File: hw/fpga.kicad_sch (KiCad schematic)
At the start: 1 part, among them U3 ICE40UL1K-CM36AITR

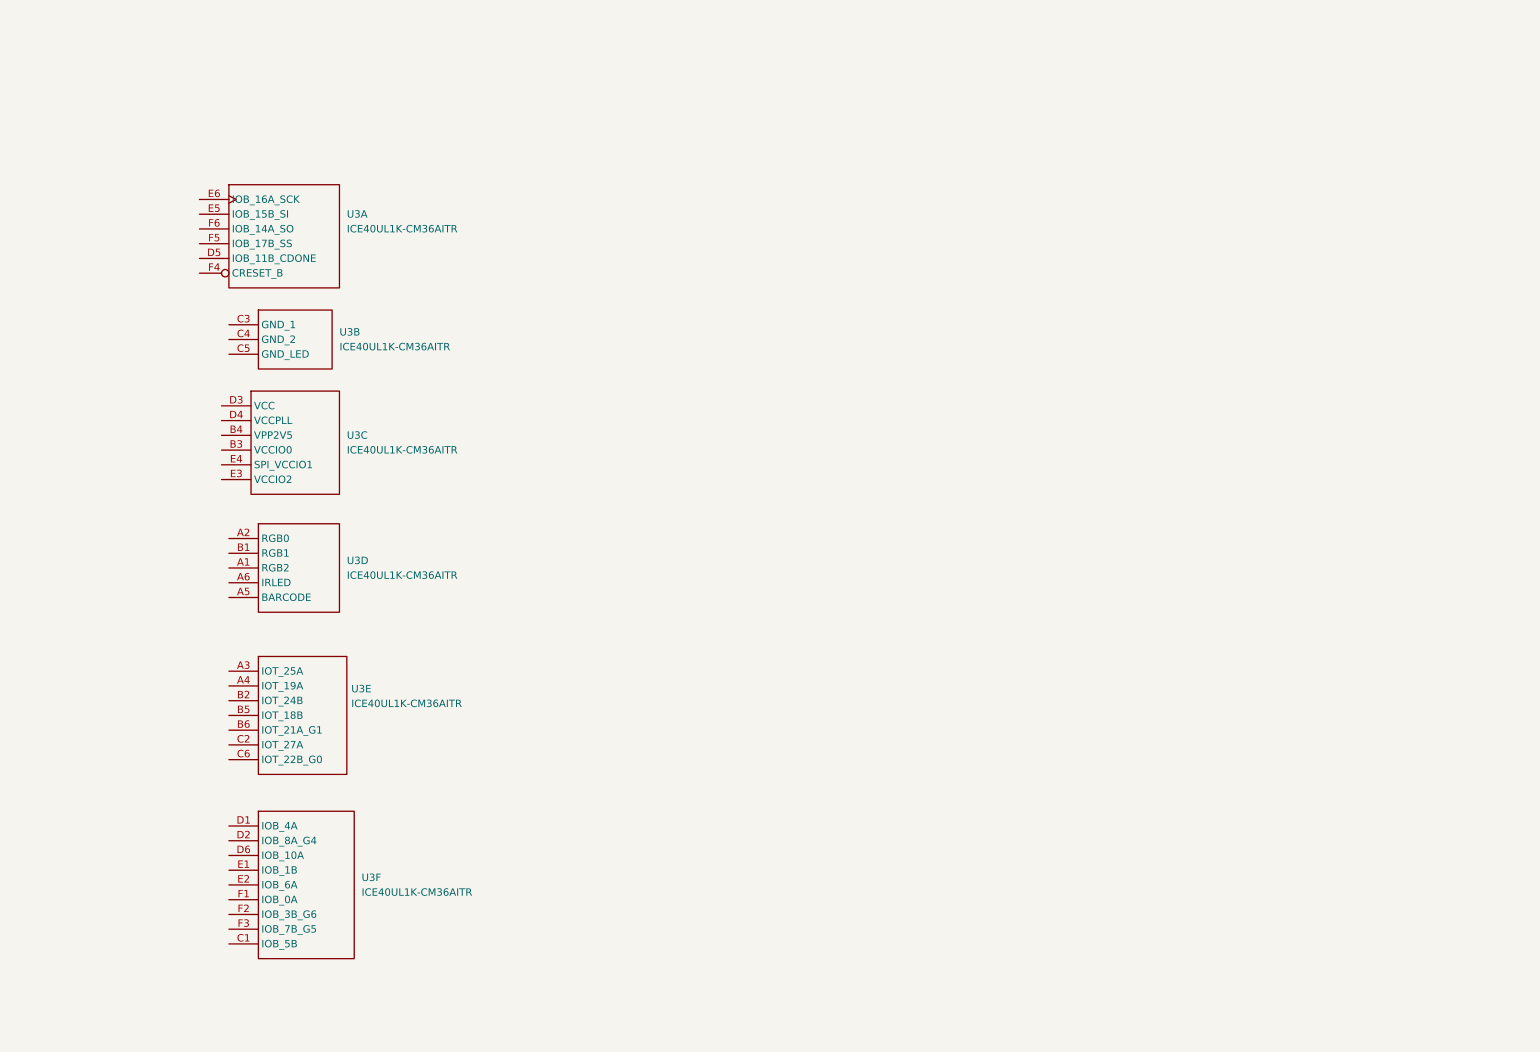
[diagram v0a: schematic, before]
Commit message: Place FPGA
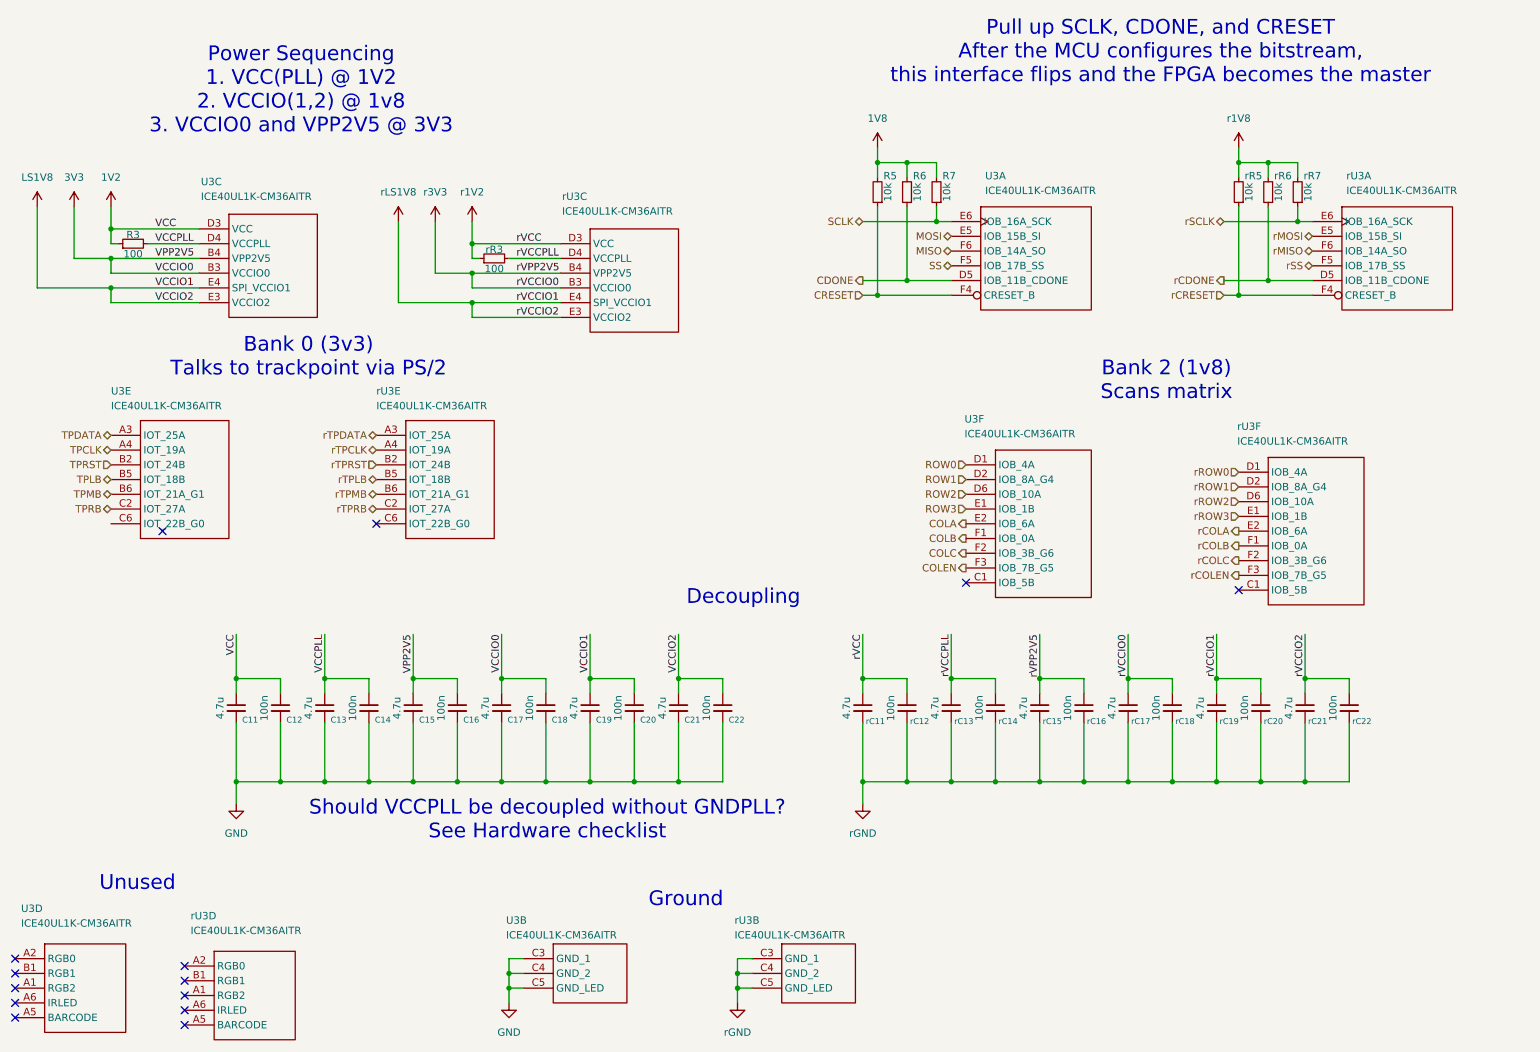
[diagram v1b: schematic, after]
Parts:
- added C11, C13, C15, C17, C19, C21, rC11, rC13, rC15, rC17, rC19, rC21: 4.7u, symbol Alidade:C
- added C12, C14, C16, C18, C20, C22, rC12, rC14, rC16, rC18, rC20, rC22: 100n, symbol Alidade:C
- added R3, rR3: 100, symbol Alidade:R
- added R5, R6, R7, rR5, rR6, rR7: 10k, symbol Alidade:R
- added rU3: ICE40UL1K-CM36AITR, Alidade:BGA36C40P6X6_250X250X100, symbol Alidade:ICE40UL1K-CM36AITR
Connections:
- net 3V3: now reaches U3.B3 (VCCIO0)
- net 3V3: now also U3.B4 (VPP2V5), C15.1, C16.1, C17.1, C18.1
- net 1V2: now reaches U3.D3 (VCC)
- net 1V2: now also C11.1, C12.1, R3.1
- net VCCPLL: now reaches U3.D4 (VCCPLL)
- net VCCPLL: now also C13.1, C14.1, R3.2
- net LS1V8: now reaches U3.E3 (VCCIO2)
- net LS1V8: now also U3.E4 (SPI_VCCIO1), C19.1, C20.1, C21.1, C22.1
- net TPDATA: now reaches U3.A3 (IOT_25A)
- net TPCLK: now reaches U3.A4 (IOT_19A)
- net TPRST: now reaches U3.B2 (IOT_24B)
- net TPLB: now reaches U3.B5 (IOT_18B)
- net TPMB: now reaches U3.B6 (IOT_21A_G1)
- net TPRB: now reaches U3.C2 (IOT_27A)
- net CDONE: now reaches U3.D5 (IOB_11B_CDONE)
- net CDONE: now also R6.1
- net MOSI: now reaches U3.E5 (IOB_15B_SI)
- net SCLK: now reaches U3.E6 (IOB_16A_SCK)
- net SCLK: now also R7.1
- net CRESET: now reaches U3.F4 (CRESET_B)
- net CRESET: now also R5.1
- net SS: now reaches U3.F5 (IOB_17B_SS)
- net MISO: now reaches U3.F6 (IOB_14A_SO)
- net ROW0: now reaches U3.D1 (IOB_4A)
- net ROW1: now reaches U3.D2 (IOB_8A_G4)
- net ROW2: now reaches U3.D6 (IOB_10A)
- net ROW3: now reaches U3.E1 (IOB_1B)
- net COLA: now reaches U3.E2 (IOB_6A)
- net COLB: now reaches U3.F1 (IOB_0A)
- net COLC: now reaches U3.F2 (IOB_3B_G6)
- net COLEN: now reaches U3.F3 (IOB_7B_G5)
- net GND: now reaches U3.C3 (GND_1)
- net GND: now also U3.C4 (GND_2), U3.C5 (GND_LED), C11.2, C12.2, C13.2, C14.2, C15.2, C16.2, C17.2, C18.2, C19.2, C20.2, C21.2, C22.2
- new net 1V8: R5.2, R6.2, R7.2
- new net r1V2: rC11.1, rC12.1, rR3.1, rU3.D3 (VCC)
- new net r1V8: rR5.2, rR6.2, rR7.2
- new net r3V3: rC15.1, rC16.1, rC17.1, rC18.1, rU3.B3 (VCCIO0), rU3.B4 (VPP2V5)
- new net rCDONE: rR6.1, rU3.D5 (IOB_11B_CDONE)
- new net rCOLA: rU3.E2 (IOB_6A)
- new net rCOLB: rU3.F1 (IOB_0A)
- new net rCOLC: rU3.F2 (IOB_3B_G6)
- new net rCOLEN: rU3.F3 (IOB_7B_G5)
- new net rCRESET: rR5.1, rU3.F4 (CRESET_B)
- new net rGND: rC11.2, rC12.2, rC13.2, rC14.2, rC15.2, rC16.2, rC17.2, rC18.2, rC19.2, rC20.2, rC21.2, rC22.2, rU3.C3 (GND_1), rU3.C4 (GND_2), rU3.C5 (GND_LED)
- new net rLS1V8: rC19.1, rC20.1, rC21.1, rC22.1, rU3.E3 (VCCIO2), rU3.E4 (SPI_VCCIO1)
- new net rMISO: rU3.F6 (IOB_14A_SO)
- new net rMOSI: rU3.E5 (IOB_15B_SI)
- new net rROW0: rU3.D1 (IOB_4A)
- new net rROW1: rU3.D2 (IOB_8A_G4)
- new net rROW2: rU3.D6 (IOB_10A)
- new net rROW3: rU3.E1 (IOB_1B)
- new net rSCLK: rR7.1, rU3.E6 (IOB_16A_SCK)
- new net rSS: rU3.F5 (IOB_17B_SS)
- new net rTPCLK: rU3.A4 (IOT_19A)
- new net rTPDATA: rU3.A3 (IOT_25A)
- new net rTPLB: rU3.B5 (IOT_18B)
- new net rTPMB: rU3.B6 (IOT_21A_G1)
- new net rTPRB: rU3.C2 (IOT_27A)
- new net rTPRST: rU3.B2 (IOT_24B)
- new net rVCCPLL: rC13.1, rC14.1, rR3.2, rU3.D4 (VCCPLL)
- no-connect marks 0 -> 14
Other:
- note added: "Bank 0 (3v3) Talks to trackpoint via PS/2"
- note added: "Bank 2 (1v8) Scans matrix"
- note added: "Decoupling"
- note added: "Ground"
- note added: "Power Sequencing 1. VCC(PLL) @ 1V2 2. VCCIO(1,2) @ 1v8 3. VCCIO0 and VPP2V5 @ 3V3"
- note added: "Pull up SCLK, CDONE, and CRESET After the MCU configures the bitstream, this interface flips and the FPGA becomes the master"
- note added: "Should VCCPLL be decoupled without GNDPLL? See Hardware checklist"
- note added: "Unused"
- moved on the sheet: U3A, U3B, U3C, U3D, U3E, U3F

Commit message: Sheet pins
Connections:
- net MISO renamed FPGAMISO
- net MOSI renamed FPGAMOSI
- net SCLK renamed FPGASCLK
- net SS renamed FPGACS
- net rMISO renamed rFPGAMISO
- net rMOSI renamed rFPGAMOSI
- net rSCLK renamed rFPGASCLK
- net rSS renamed rFPGACS
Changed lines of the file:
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@@
 	)
 	(no_connect
-		(at 49.53 104.14)
+		(at 40.64 102.87)
 	)
 	(no_connect
@@
 	(wire
 		(pts
+			(xy 170.18 55.88) (xy 185.42 55.88)
+		)
+		(stroke
+			(width 0)
+			(type default)
+		)
+	)
+	(wire
+		(pts
 			(xy 107.95 137.16) (xy 107.95 147.32)
 		)
@@
 	(wire
 		(pts
+			(xy 170.18 58.42) (xy 185.42 58.42)
+		)
+		(stroke
+			(width 0)
+			(type default)
+		)
+	)
+	(wire
+		(pts
 			(xy 118.11 64.77) (xy 102.87 64.77)
 		)
@@
 	(wire
 		(pts
+			(xy 170.18 53.34) (xy 185.42 53.34)
+		)
+		(stroke
+			(width 0)
+			(type default)
+		)
+	)
+	(wire
+		(pts
 			(xy 55.88 64.77) (xy 40.64 64.77)
 		)
@@
 	(wire
 		(pts
+			(xy 232.41 53.34) (xy 247.65 53.34)
+		)
+		(stroke
+			(width 0)
+			(type default)
+		)
+	)
+	(wire
+		(pts
 			(xy 151.13 182.88) (xy 148.59 182.88)
 		)
@@
 	(wire
 		(pts
+			(xy 232.41 55.88) (xy 247.65 55.88)
+		)
+		(stroke
+			(width 0)
+			(type default)
+		)
+	)
+	(wire
+		(pts
 			(xy 200.66 121.92) (xy 200.66 129.54)
 		)
@@
 		(pts
 			(xy 92.71 121.92) (xy 92.71 129.54)
+		)
+		(stroke
+			(width 0)
+			(type default)
+		)
+	)
+	(wire
+		(pts
+			(xy 232.41 58.42) (xy 247.65 58.42)
 		)
 		(stroke
@@
 		)
 	)
-	(hierarchical_label "rMOSI"
+	(hierarchical_label "rFPGAMOSI"
 		(shape bidirectional)
-		(at 247.65 53.34 180)
+		(at 232.41 53.34 180)
 		(effects
 			(font
@@
 		)
 	)
-	(hierarchical_label "MISO"
+	(hierarchical_label "FPGAMISO"
 		(shape bidirectional)
-		(at 185.42 55.88 180)
+		(at 170.18 55.88 180)
 		(effects
 			(font
@@
 		)
 	)
-	(hierarchical_label "SCLK"
+	(hierarchical_label "FPGASCLK"
 		(shape bidirectional)
 		(at 170.18 50.8 180)
@@
 		)
 	)
-	(hierarchical_label "rSCLK"
+	(hierarchical_label "rFPGASCLK"
 		(shape bidirectional)
 		(at 232.41 50.8 180)
@@
 		)
 	)
-	(hierarchical_label "rMISO"
+	(hierarchical_label "rFPGAMISO"
 		(shape bidirectional)
-		(at 247.65 55.88 180)
+		(at 232.41 55.88 180)
 		(effects
 			(font
@@
 		)
 	)
-	(hierarchical_label "MOSI"
+	(hierarchical_label "FPGAMOSI"
 		(shape bidirectional)
-		(at 185.42 53.34 180)
+		(at 170.18 53.34 180)
 		(effects
 			(font
@@
 		)
 	)
-	(hierarchical_label "rSS"
+	(hierarchical_label "rFPGACS"
 		(shape bidirectional)
-		(at 247.65 58.42 180)
+		(at 232.41 58.42 180)
 		(effects
 			(font
@@
 		)
 	)
-	(hierarchical_label "SS"
+	(hierarchical_label "FPGACS"
 		(shape bidirectional)
-		(at 185.42 58.42 180)
-		(effects
-			(font
+		(at 170.18 58.42 180)
+		(effects
+			(font

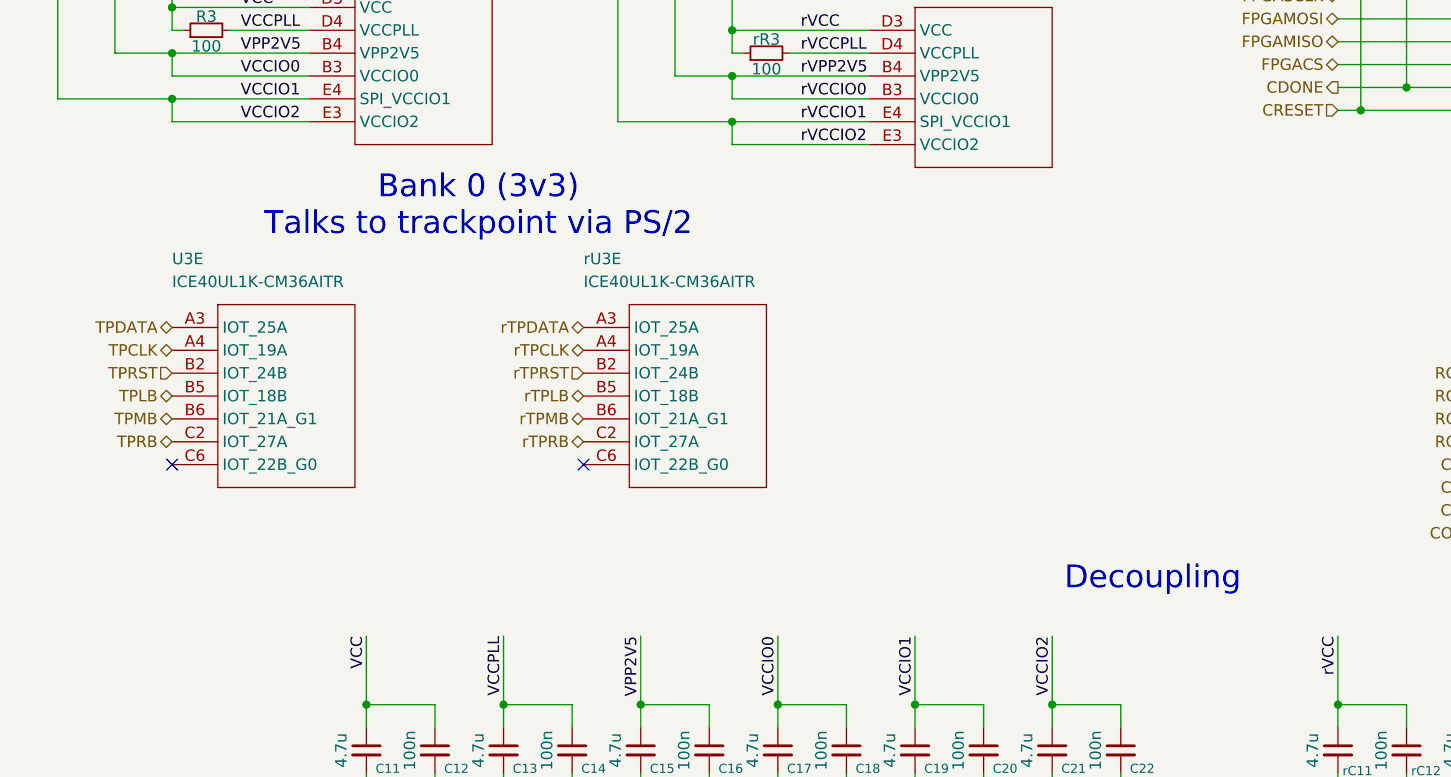
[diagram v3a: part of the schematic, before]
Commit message: Place and connect trackpoint module
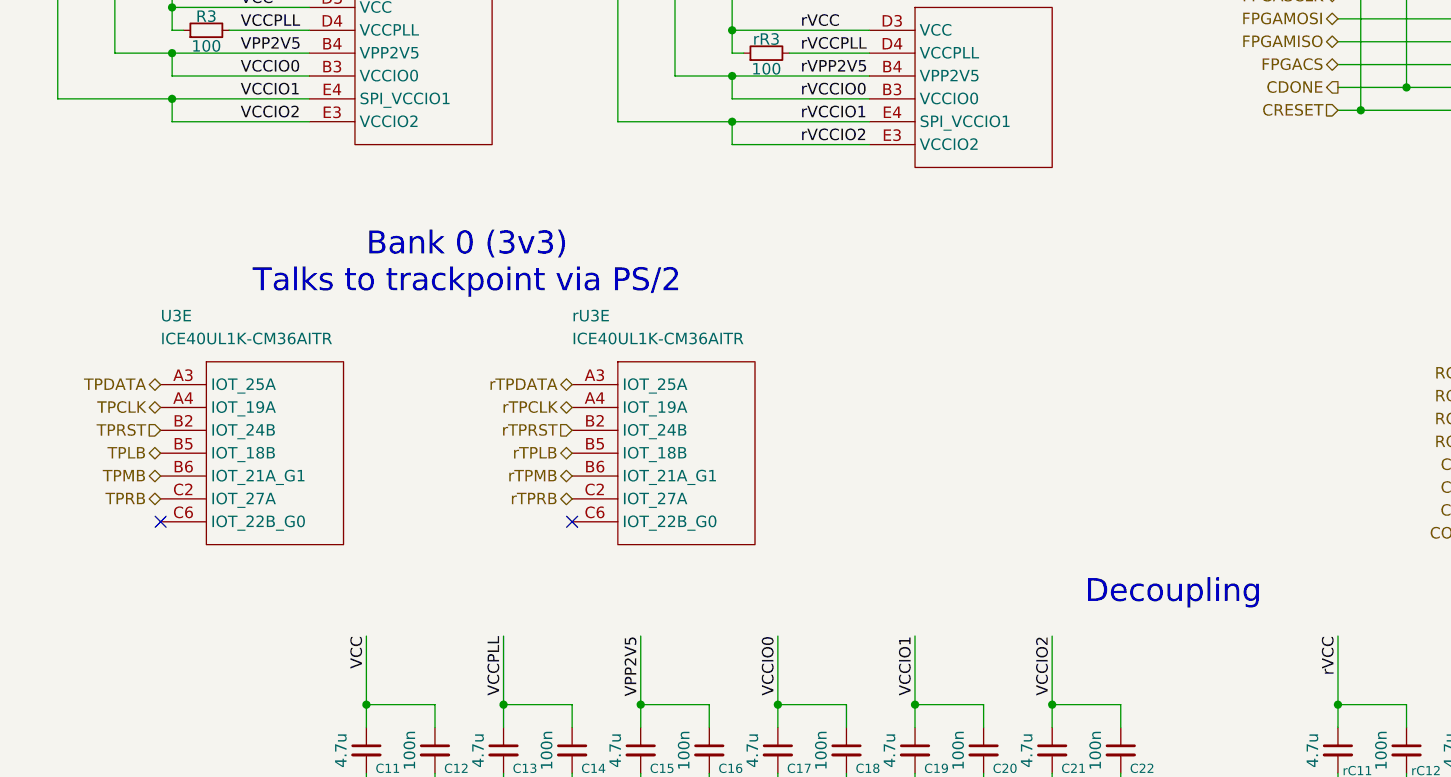
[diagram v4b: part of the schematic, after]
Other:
- moved on the sheet: U3E, rU3E
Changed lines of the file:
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@@
 	(text "Decoupling"
 		(exclude_from_sim no)
-		(at 149.606 115.57 0)
+		(at 151.892 117.094 0)
 		(effects
 			(font
@@
 	(text "Bank 0 (3v3)\nTalks to trackpoint via PS/2"
 		(exclude_from_sim no)
-		(at 74.676 74.168 0)
+		(at 73.406 80.518 0)
 		(effects
 			(font
@@
 	)
 	(no_connect
-		(at 86.36 102.87)
+		(at 85.09 109.22)
 	)
 	(no_connect
@@
 	)
 	(no_connect
-		(at 40.64 102.87)
+		(at 39.37 109.22)
 	)
 	(no_connect
@@
 	(hierarchical_label "rTPMB"
 		(shape bidirectional)
-		(at 86.36 97.79 180)
+		(at 85.09 104.14 180)
 		(effects
 			(font
@@
 	(hierarchical_label "rTPDATA"
 		(shape bidirectional)
-		(at 86.36 87.63 180)
+		(at 85.09 93.98 180)
 		(effects
 			(font
@@
 	(hierarchical_label "rTPCLK"
 		(shape bidirectional)
-		(at 86.36 90.17 180)
+		(at 85.09 96.52 180)
 		(effects
 			(font
@@
 	(hierarchical_label "TPCLK"
 		(shape bidirectional)
-		(at 40.64 90.17 180)
+		(at 39.37 96.52 180)
 		(effects
 			(font
@@
 	(hierarchical_label "TPRST"
 		(shape input)
-		(at 40.64 92.71 180)
+		(at 39.37 99.06 180)
 		(effects
 			(font
@@
 	(hierarchical_label "TPRB"
 		(shape bidirectional)
-		(at 40.64 100.33 180)
+		(at 39.37 106.68 180)
 		(effects
 			(font
@@
 	(hierarchical_label "rTPRST"
 		(shape input)
-		(at 86.36 92.71 180)
+		(at 85.09 99.06 180)
 		(effects
 			(font
@@
 	(hierarchical_label "rTPRB"
 		(shape bidirectional)
-		(at 86.36 100.33 180)
+		(at 85.09 106.68 180)
 		(effects
 			(font
@@
 	(hierarchical_label "TPLB"
 		(shape bidirectional)
-		(at 40.64 95.25 180)
+		(at 39.37 101.6 180)
 		(effects
 			(font
@@
 	(hierarchical_label "TPDATA"
 		(shape bidirectional)
-		(at 40.64 87.63 180)
+		(at 39.37 93.98 180)
 		(effects
 			(font
@@
 	(hierarchical_label "TPMB"
 		(shape bidirectional)
-		(at 40.64 97.79 180)
+		(at 39.37 104.14 180)
 		(effects
 			(font
@@
 	(hierarchical_label "rTPLB"
 		(shape bidirectional)
-		(at 86.36 95.25 180)
+		(at 85.09 101.6 180)
 		(effects
 			(font
@@
 	(symbol
 		(lib_id "Alidade:ICE40UL1K-CM36AITR")
-		(at 86.36 85.09 0)
+		(at 85.09 91.44 0)
 		(unit 5)
 		(exclude_from_sim no)
@@
 		(dnp no)
 		(property "Reference" "rU3"
-			(at 86.36 80.01 0)
+			(at 85.09 86.36 0)
 			(effects
 				(font
@@
 		)
 		(property "Value" "ICE40UL1K-CM36AITR"
-			(at 86.36 82.55 0)
+			(at 85.09 88.9 0)
 			(effects
 				(font
@@
 		)
 		(property "Footprint" "Alidade:BGA36C40P6X6_250X250X100"
-			(at 90.424 68.072 0)
+			(at 89.154 74.422 0)
 			(effects
 				(font
@@
 		)
 		(property "Datasheet" "https://www.latticesemi.com/-/media/LatticeSemi/Documents/DataSheets/iCE/FPGA-DS-02027-1-9-iCE40-UltraLite-Family-Data-Sheet.ashx?document_id=50945"
-			(at 89.662 72.898 0)
+			(at 88.392 79.248 0)
 			(effects
 				(font
@@
 		)
 		(property "Description" ""
-			(at 147.32 174.244 0)
+			(at 146.05 180.594 0)
 			(effects
 				(font
@@
 	(symbol
 		(lib_id "Alidade:ICE40UL1K-CM36AITR")
-		(at 40.64 85.09 0)
+		(at 39.37 91.44 0)
 		(unit 5)
 		(exclude_from_sim no)
@@
 		(dnp no)
 		(property "Reference" "U3"
-			(at 40.64 80.01 0)
+			(at 39.37 86.36 0)
 			(effects
 				(font
@@
 		)
 		(property "Value" "ICE40UL1K-CM36AITR"
-			(at 40.64 82.55 0)
+			(at 39.37 88.9 0)
 			(effects
 				(font
@@
 		)
 		(property "Footprint" "Alidade:BGA36C40P6X6_250X250X100"
-			(at 44.704 68.072 0)
+			(at 43.434 74.422 0)
 			(effects
 				(font
@@
 		)
 		(property "Datasheet" "https://www.latticesemi.com/-/media/LatticeSemi/Documents/DataSheets/iCE/FPGA-DS-02027-1-9-iCE40-UltraLite-Family-Data-Sheet.ashx?document_id=50945"
-			(at 43.942 72.898 0)
+			(at 42.672 79.248 0)
 			(effects
 				(font
@@
 		)
 		(property "Description" ""
-			(at 101.6 174.244 0)
+			(at 100.33 180.594 0)
 			(effects
 				(font
